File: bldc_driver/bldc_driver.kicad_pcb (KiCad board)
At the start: 2 copper layers, 74.9 x 56.1 mm, 77 parts, among them CON1 SAM-SWD-10, J1 I2C 1, Q1 PSMN0R925YLC, Q10 PSMN0R925YLC, Q11 PSMN0R925YLC, Q12 PSMN0R925YLC, Q2 PSMN0R925YLC, Q3 PSMN0R925YLC, Q4 PSMN0R925YLC, Q5 PSMN0R925YLC, Q6 PSMN0R925YLC, Q7 PSMN0R925YLC, Q8 PSMN0R925YLC, Q9 PSMN0R925YLC, U1 SAMD21E16L-MU, U2 INA199A2, U3 NCP5901, U4 NCP5901, U5 NCP5901, U6 INA199A2, U7 NCP5901, U8 NCP5901, U9 NCP5901

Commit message: well, missed commit when I fabricated the board, but I have extra parts here to try to fix it... honestly, I should just redesign with mosfet drivers intended for motor use that tolerate negative voltages
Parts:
- C10, C11, C12, C20, C21, C22: value 360nF -> 470nF
- R10, R11, R12, R17, R18, R19: value 4k -> 4.02k
- R2: value 3.9k -> 4.02k
- R5: value 1k -> 3k
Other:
- net class POWER_DRIVE added: clearance 0.2, trace_width 2, via_dia 0.6, via_drill 0.4

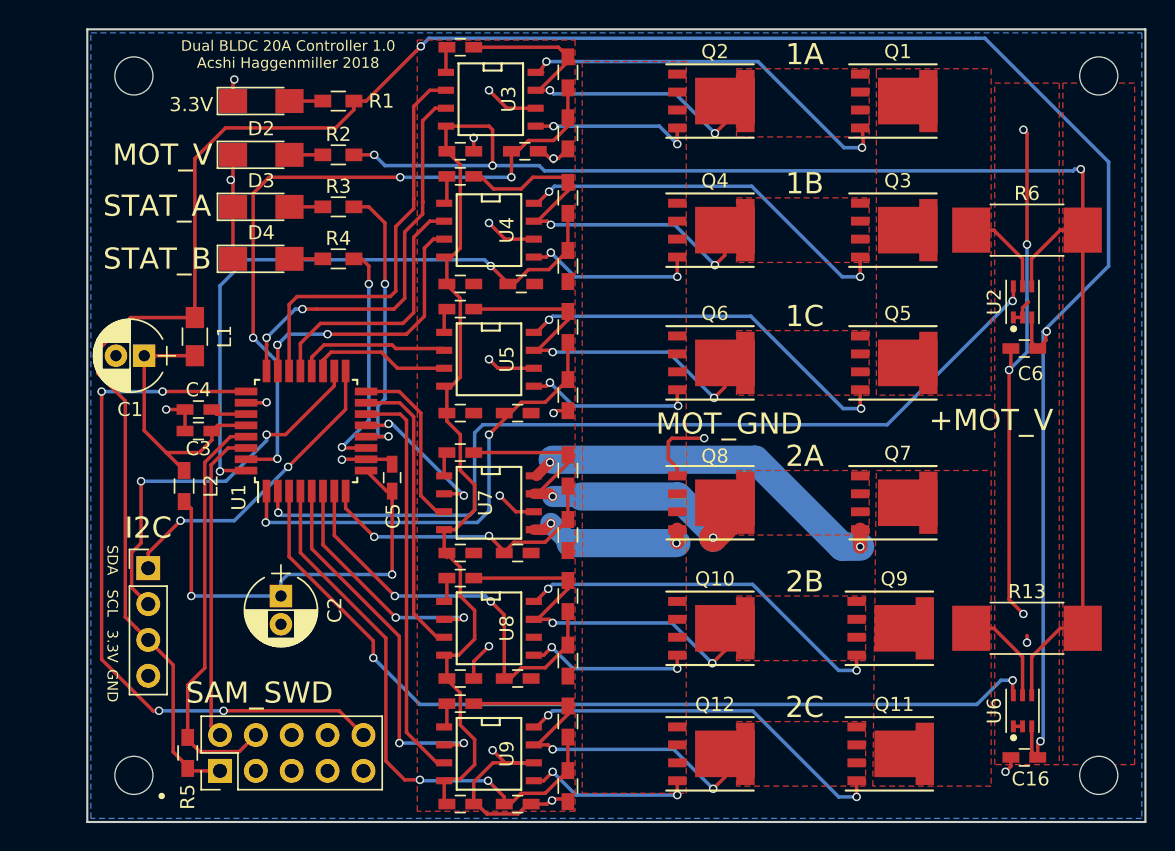
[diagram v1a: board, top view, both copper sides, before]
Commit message: finished v1.1 bldc, sent to make pcb; added components to quad rotor main board
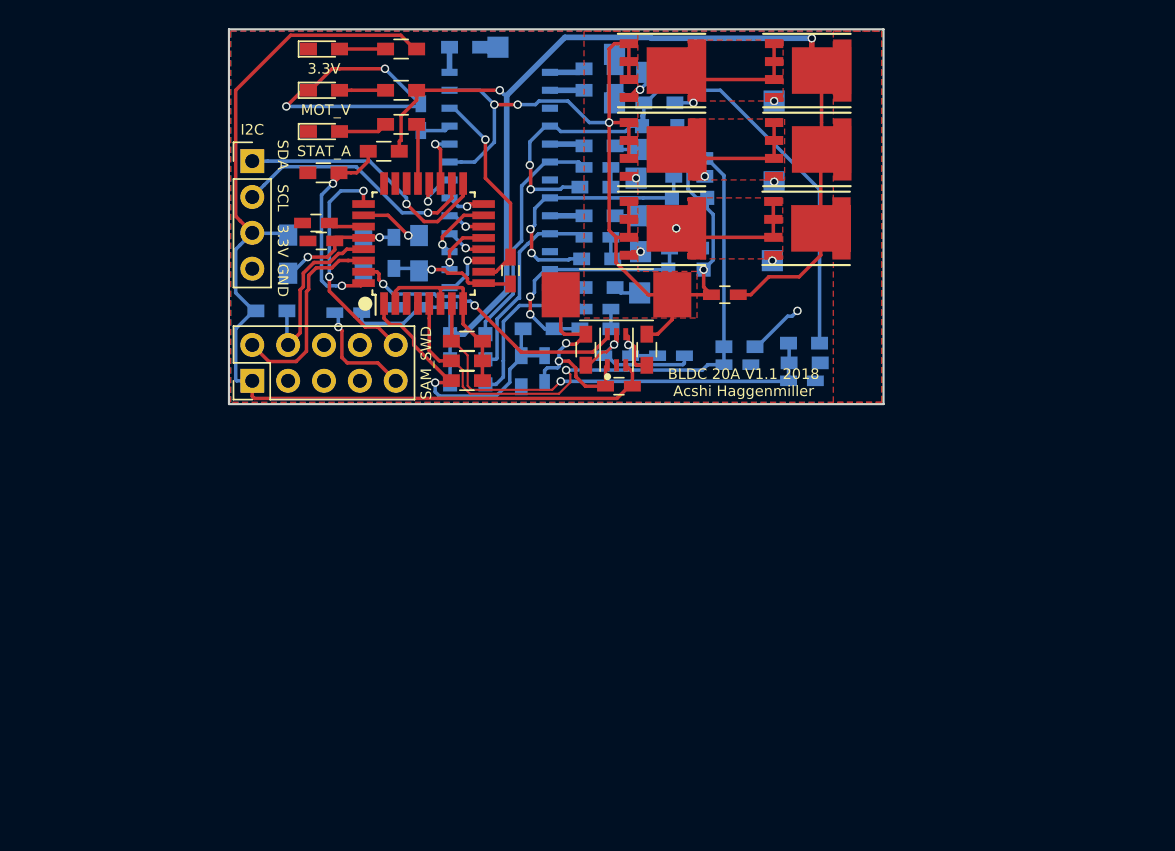
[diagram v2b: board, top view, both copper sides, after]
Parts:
- removed C20, C21, C22: 470nF, Capacitors_SMD:C_0603_HandSoldering
- removed C23, C24, C25: 1nF, Capacitors_SMD:C_0603_HandSoldering
- removed C6: 100nF, Capacitors_SMD:C_0603_HandSoldering
- removed Q10, Q11, Q12, Q7, Q8, Q9: PSMN0R925YLC, LFPAK:LFPAK_POWER_SO-8
- removed the REF** at (114.6, 125.2)
- removed the REF** at (114.6, 75.7)
- removed the REF** at (182.9, 75.7)
- removed the REF** at (182.9, 125.2)
- removed U4, U5, U7, U8, U9: NCP5901, SMD_Packages:SOIC-8-N
- removed U6: INA199A2, ina199a2:INA199A2
- added D5: DSS16UTR‎, Diodes_SMD:D_SOD-323_HandSoldering, B.Cu at (153.9, 84.3)
- added D6: DSS16UTR‎, Diodes_SMD:D_SOD-323_HandSoldering, B.Cu at (151.8, 79.2)
- added D7: DSS16UTR‎, Diodes_SMD:D_SOD-323_HandSoldering, B.Cu at (138.2, 94.0)
- added D8: DSS16UTR‎, Diodes_SMD:D_SOD-323_HandSoldering, B.Cu at (138.2, 95.8)
- added D9: DSS16UTR‎, Diodes_SMD:D_SOD-323_HandSoldering, B.Cu at (138.2, 97.5)
- added R20: 1R, Resistors_SMD:R_0603_HandSoldering, B.Cu at (147.2, 93.6)
- added R21: 1R, Resistors_SMD:R_0603_HandSoldering, B.Cu at (147.4, 88.6)
- added R22: 1R, Resistors_SMD:R_0603_HandSoldering, B.Cu at (147.2, 83.6)
- added R23: 20k, Resistors_SMD:R_0603_HandSoldering, B.Cu at (143.2, 93.6)
- added R24: 20k, Resistors_SMD:R_0603_HandSoldering, B.Cu at (153.9, 81.5)
- added R25: 20k, Resistors_SMD:R_0603_HandSoldering, B.Cu at (162.0, 94.6)
- added R26: 4.02k, Resistors_SMD:R_0603_HandSoldering, B.Cu at (142.0, 96.6)
- added R27: 4.02k, Resistors_SMD:R_0603_HandSoldering, B.Cu at (157.4, 94.9)
- added R28: 4.02k, Resistors_SMD:R_0603_HandSoldering, B.Cu at (162.1, 96.0)
- added R29: 20k, Resistors_SMD:R_0603_HandSoldering, F.Cu at (132.2, 81.0)
- added R30: 4.02k, Resistors_SMD:R_0603_HandSoldering, F.Cu at (128.0, 82.5)
- added REF**: Measurement_Point_Square-SMD-Pad_Small, Measurement_Points:Measurement_Point_Square-SMD-Pad_Small, B.Cu at (159.9, 83.2)
- added REF**: Measurement_Point_Square-SMD-Pad_Small, Measurement_Points:Measurement_Point_Square-SMD-Pad_Small, B.Cu at (148.6, 77.6)
- added REF**: Measurement_Point_Square-SMD-Pad_Small, Measurement_Points:Measurement_Point_Square-SMD-Pad_Small, B.Cu at (150.1, 82.9)
- added REF**: Measurement_Point_Square-SMD-Pad_Small, Measurement_Points:Measurement_Point_Square-SMD-Pad_Small, B.Cu at (140.3, 73.7)
- added REF**: Measurement_Point_Square-SMD-Pad_Small, Measurement_Points:Measurement_Point_Square-SMD-Pad_Small, B.Cu at (159.9, 77.5)
- added REF**: Measurement_Point_Square-SMD-Pad_Small, Measurement_Points:Measurement_Point_Square-SMD-Pad_Small, B.Cu at (159.8, 88.8)
- added REF**: Measurement_Point_Square-SMD-Pad_Small, Measurement_Points:Measurement_Point_Square-SMD-Pad_Small, B.Cu at (150.4, 88.1)
- added REF**: Measurement_Point_Square-SMD-Pad_Small, Measurement_Points:Measurement_Point_Square-SMD-Pad_Small, B.Cu at (150.4, 91.1)
- added REF**: Measurement_Point_Square-SMD-Pad_Small, Measurement_Points:Measurement_Point_Square-SMD-Pad_Small, B.Cu at (150.4, 85.6)
- added REF**: Measurement_Point_Square-SMD-Pad_Small, Measurement_Points:Measurement_Point_Square-SMD-Pad_Small, B.Cu at (150.4, 80.9)
- added REF**: Measurement_Point_Square-SMD-Pad_Small, Measurement_Points:Measurement_Point_Square-SMD-Pad_Small, B.Cu at (150.9, 75.4)
- added REF**: Measurement_Point_Square-SMD-Pad_Small, Measurement_Points:Measurement_Point_Square-SMD-Pad_Small, B.Cu at (148.6, 74.2)
- C1, C2: footprint Capacitors_THT:CP_Radial_D5.0mm_P2.00mm -> Capacitors_SMD:C_0805_HandSoldering; moved to B.Cu
- C10: value 470nF -> 1uF; moved to B.Cu
- C11: value 470nF -> 100nF
- C12: value 470nF -> 1nF; moved to B.Cu
- C13: value 1nF -> 1uF; moved to B.Cu
- C14, C15: value 1nF -> 0.68uF; moved to B.Cu
- C16: value 100nF -> 0.68uF; moved to B.Cu
- C17, C18, C19: value 100n -> 1nF; moved to B.Cu
- C7: value 100n -> 100nF
- C8, C9: value 100n -> 1uF; moved to B.Cu
- D1, D2, D3: footprint LEDs:LED_1206_HandSoldering -> LEDs:LED_0603_HandSoldering
- D4: value Red -> DSS16UTR‎; footprint LEDs:LED_1206_HandSoldering -> Diodes_SMD:D_SOD-323_HandSoldering; moved to B.Cu
- L1, L2, R4: moved to B.Cu
- R10, R12: value 4.02k -> 10
- R11: value 4.02k -> 2mR; footprint Resistors_SMD:R_0603_HandSoldering -> Resistors_SMD:R_2512_HandSoldering
- R13: value 2mR -> 10; footprint Resistors_SMD:R_2512_HandSoldering -> Resistors_SMD:R_0603_HandSoldering; moved to B.Cu
- R14, R15, R16: value 20k -> 4.7R; moved to B.Cu
- R17, R18, R19: value 4.02k -> 4.7R; moved to B.Cu
- R6: value 2mR -> 3k; footprint Resistors_SMD:R_2512_HandSoldering -> Resistors_SMD:R_0603_HandSoldering
- R7, R9: value 20k -> 10; moved to B.Cu
- R8: value 20k -> 3k
- U2: value INA199A2 -> INA199C2
- U3: value NCP5901 -> MIC4609; footprint SMD_Packages:SOIC-8-N -> SMD_Packages:SOIC-28; moved to B.Cu
- moved R19 52.8 mm to (138.0, 73.7), turned to 180 degrees
- moved C16 51.6 mm to (147.4, 82.2)
- moved R13 45.4 mm to (151.8, 77.6), turned to 180 degrees
- moved R18 42.0 mm to (147.5, 75.2), turned to 180 degrees
- moved R16 40.8 mm to (147.5, 80.6), turned to 180 degrees
- moved R6 40.7 mm to (138.1, 95.9), turned to 180 degrees
- moved C19 38.5 mm to (161.9, 97.3)
- moved R5 33.0 mm to (138.1, 97.3), turned to 180 degrees
- moved R17 31.6 mm to (147.5, 76.7), turned to 180 degrees
- moved D4 30.1 mm to (153.7, 89.4)
- moved J1 29.8 mm to (122.9, 81.7)
- moved C18 29.6 mm to (157.3, 96.1)
- moved U2 28.9 mm to (148.7, 95.1)
- moved CON1 27.7 mm to (122.9, 97.3)
- moved R15 27.0 mm to (147.5, 85.6), turned to 180 degrees
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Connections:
- C10 pad 1: Net-(C10-Pad1) -> GND
- C10 pad 2: /bldc_unit1/MOT_A -> /+V_MOTOR
- C11 pad 1: Net-(C11-Pad1) -> GND
- C11 pad 2: /bldc_unit1/MOT_B -> /+3.3V
- C12 pad 1: Net-(C12-Pad1) -> GND
- C12 pad 2: /bldc_unit1/MOT_C -> Net-(C12-Pad2)
- C13 pad 1: /bldc_unit1/MOTOR_A -> GND
- C13 pad 2: GND -> /+V_MOTOR
- C14 pad 1: /bldc_unit1/MOTOR_B -> Net-(C14-Pad1)
- C14 pad 2: GND -> Net-(C14-Pad2)
- C15 pad 1: /MOTOR1_C -> Net-(C15-Pad1)
- C15 pad 2: GND -> Net-(C15-Pad2)
- C16 pad 1: GND -> Net-(C16-Pad1)
- C16 pad 2: /+3.3V -> Net-(C16-Pad2)
- C17 pad 1: /+V_MOTOR -> /bldc_unit1/MOTOR_A
- C18 pad 1: /+V_MOTOR -> /bldc_unit1/MOTOR_B
- C19 pad 1: /+V_MOTOR -> /bldc_unit1/MOTOR_C
- C7 pad 2: GND -> /bldc_unit1/MOTOR_SHUNT
- C8 pad 1: /+V_MOTOR -> Net-(C8-Pad1)
- C8 pad 2: GND -> Net-(C8-Pad2)
- C9 pad 1: /+V_MOTOR -> Net-(C8-Pad1)
- C9 pad 2: GND -> Net-(C8-Pad2)
- CON1 pad 6: Net-(CON1-Pad6) -> (no net)
- CON1 pad 7: Net-(CON1-Pad7) -> (no net)
- CON1 pad 8: Net-(CON1-Pad8) -> (no net)
- D4 pad 1: GND -> /bldc_unit1/MOTF_A
- D4 pad 2: Net-(D4-Pad2) -> /bldc_unit1/MOTOR_SHUNT
- Q1 pad 1: /bldc_unit1/MOTOR_SHUNT -> /+V_MOTOR
- Q2 pad 3: GND -> /bldc_unit1/MOTOR_SHUNT
- Q3 pad 1: /bldc_unit1/MOTOR_SHUNT -> /+V_MOTOR
- Q4 pad 3: GND -> /bldc_unit1/MOTOR_SHUNT
- Q5 pad 1: /bldc_unit1/MOTOR_SHUNT -> /+V_MOTOR
- Q6 pad 3: GND -> /bldc_unit1/MOTOR_SHUNT
- R10 pad 1: GND -> Net-(C8-Pad2)
- R10 pad 2: /bldc_unit1/MOTOR_A -> /bldc_unit1/MOTOR_SHUNT
- R11 pad 1: /bldc_unit1/MOTOR_B -> GND
- R11 pad 2: GND -> /bldc_unit1/MOTOR_SHUNT
- R12 pad 1: /MOTOR1_C -> Net-(C8-Pad1)
- R13 pad 1: /bldc_unit2/MOTOR_SHUNT -> /bldc_unit1/MOT_C
- R13 pad 2: /+V_MOTOR -> /bldc_unit1/MOTF_C
- R14 pad 1: /bldc_unit2/MOTOR_A -> /bldc_unit1/GHA
- R14 pad 2: /bldc_unit2/MOT_A -> Net-(R14-Pad2)
- R15 pad 1: /bldc_unit2/MOTOR_B -> /bldc_unit1/GHB
- R15 pad 2: /bldc_unit2/MOT_B -> Net-(R15-Pad2)
- R16 pad 1: /MOTOR2_C -> /bldc_unit1/GHC
- R16 pad 2: /bldc_unit2/MOT_C -> Net-(R16-Pad2)
- R17 pad 1: GND -> /bldc_unit1/GLA
- R17 pad 2: /bldc_unit2/MOTOR_A -> Net-(R17-Pad2)
- R18 pad 1: /bldc_unit2/MOTOR_B -> /bldc_unit1/GLB
- R18 pad 2: GND -> Net-(R18-Pad2)
- R19 pad 1: /MOTOR2_C -> /bldc_unit1/GLC
- R19 pad 2: GND -> Net-(R19-Pad2)
- R3 pad 2: /STATUS_A -> /STATUS
- R4 pad 1: Net-(D4-Pad2) -> /+3.3V
- R4 pad 2: /STATUS_B -> /SWCLK
- R5 pad 1: /+3.3V -> /bldc_unit1/MOTOR_ZERO
- R5 pad 2: /SWCLK -> /bldc_unit1/MOTOR_A
- R6 pad 1: /bldc_unit1/MOTOR_SHUNT -> /bldc_unit1/MOTOR_ZERO
- R6 pad 2: /+V_MOTOR -> /bldc_unit1/MOTOR_B
- R7 pad 1: /bldc_unit1/MOTOR_A -> /bldc_unit1/MOTF_A
- R8 pad 1: /bldc_unit1/MOTOR_B -> /bldc_unit1/MOTOR_ZERO
- R8 pad 2: /bldc_unit1/MOT_B -> /bldc_unit1/MOTOR_C
- R9 pad 1: /MOTOR1_C -> /bldc_unit1/MOT_B
- R9 pad 2: /bldc_unit1/MOT_C -> /bldc_unit1/MOTF_B
- U1 pad 1: /MOTOR1_C -> /bldc_unit1/MOTOR_A
- U1 pad 11: /STATUS_B -> /bldc_unit1/IN_HA
- U1 pad 12: /STATUS_A -> /bldc_unit1/IN_LA
- U1 pad 13: /bldc_unit2/IN_A -> /bldc_unit1/IN_HB
- U1 pad 14: /bldc_unit2/ENABLE_C -> /bldc_unit1/IN_LB
- U1 pad 15: /bldc_unit2/ENABLE_B -> /bldc_unit1/IN_HC
- U1 pad 16: /bldc_unit2/ENABLE_A -> /bldc_unit1/IN_LC
- U1 pad 19: /bldc_unit1/ENABLE_C -> /bldc_unit1/ENABLE
- U1 pad 2: /CURRENT1 -> /bldc_unit1/MOTOR_ZERO
- U1 pad 20: /bldc_unit1/IN_C -> /bldc_unit1/~FAULT
- U1 pad 21: /bldc_unit1/IN_B -> /STATUS
- U1 pad 22: /bldc_unit1/IN_A -> (no net)
- U1 pad 23: /bldc_unit1/ENABLE_B -> (no net)
- U1 pad 24: /bldc_unit1/ENABLE_A -> (no net)
- U1 pad 3: /CURRENT2 -> (no net)
- U1 pad 31: /bldc_unit1/MOTOR_A -> /bldc_unit1/CURRENT
- U1 pad 32: /bldc_unit1/MOTOR_B -> Net-(R29-Pad2)
- U1 pad 4: /MOTOR2_C -> (no net)
- U1 pad 5: /bldc_unit2/IN_C -> /bldc_unit1/MOTOR_B
- U1 pad 6: /bldc_unit2/IN_B -> /bldc_unit1/MOTOR_ZERO
- U1 pad 7: /bldc_unit2/MOTOR_B -> /bldc_unit1/MOTOR_C
- U1 pad 8: /bldc_unit2/MOTOR_A -> /bldc_unit1/MOTOR_ZERO
- U2 pad 4: /+V_MOTOR -> Net-(C8-Pad2)
- U2 pad 5: /bldc_unit1/MOTOR_SHUNT -> Net-(C8-Pad1)
- U2 pad 6: /CURRENT1 -> /bldc_unit1/CURRENT
- U3 pad 1: Net-(C10-Pad1) -> /+V_MOTOR
- U3 pad 2: /bldc_unit1/IN_A -> /bldc_unit1/IN_HA
- U3 pad 3: /bldc_unit1/ENABLE_A -> /bldc_unit1/IN_HB
- U3 pad 4: /+V_MOTOR -> /bldc_unit1/IN_HC
- U3 pad 5: /bldc_unit1/GLA -> /bldc_unit1/IN_LA
- U3 pad 6: GND -> /bldc_unit1/IN_LB
- U3 pad 7: /bldc_unit1/MOT_A -> /bldc_unit1/IN_LC
- U3 pad 8: /bldc_unit1/GHA -> /bldc_unit1/~FAULT
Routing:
- net /+3.3V: track 176.3 -> 71.4 mm, vias 3 -> 0
- net /+V_MOTOR: track 162.3 -> 91.1 mm, vias 3 -> 2
- net /bldc_unit1/MOTOR_SHUNT: track 6.42 -> 71.6 mm, vias 0 -> 4
- net /CURRENT1: track 64.0 -> 0.00 mm, vias 2 -> 0
- net /CURRENT2: track 62.9 -> 0.00 mm, vias 2 -> 0
- net /bldc_unit1/MOTF_C: track 0.00 -> 44.9 mm, vias 0 -> 2
- net /MOTOR2_C: track 39.6 -> 0.00 mm, vias 2 -> 0
- net /MOTOR1_C: track 34.3 -> 0.00 mm, vias 2 -> 0
- net /RESET: track 50.0 -> 16.3 mm, vias 4 -> 2
- net GND: track 101.5 -> 69.2 mm, vias 21 -> 8
- net /bldc_unit1/MOTOR_C: track 0.00 -> 32.2 mm, vias 0 -> 1
- net /bldc_unit2/MOTOR_B: track 29.9 -> 0.00 mm, vias 2 -> 0
- net /bldc_unit1/IN_A: track 29.0 -> 0.00 mm
- net /bldc_unit2/ENABLE_C: track 28.7 -> 0.00 mm
- net /bldc_unit1/ENABLE_A: track 28.5 -> 0.00 mm, vias 2 -> 0
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- removed copper zone on F.Cu, net /bldc_unit2/MOTOR_SHUNT
- removed copper zone on F.Cu, net /bldc_unit2/MOT_A
- removed copper zone on F.Cu, net /bldc_unit2/MOT_B
- removed copper zone on F.Cu, net /bldc_unit2/MOT_C
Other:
- board size 74.9 x 56.1 mm -> 46.4 x 26.5 mm
- net class Default: clearance 0.2 -> 0.13
- net class POWER_DRIVE removed
- rule pad_to_mask_clearance: 0.2 -> 0.06
- rule trace_clearance: 0.2 -> 0.13
- rule trace_min: 0.2 -> 0.15
- board text added: "1"
- board text added: "2"
- board text added: "3"
- board text added: "4"
- board text added: "5"
- board text added: "6"
- board text added: "BLDC 20A V1.1 2018 Acshi Haggenmiller"
- board text removed: "+MOT_V"
- board text removed: "1A"
- board text removed: "1B"
- board text removed: "1C"
- board text removed: "2A"
- board text removed: "2B"
- board text removed: "2C"
- board text removed: "Dual BLDC 20A Controller 1.0 Acshi Haggenmiller 2018"
- board text removed: "MOT_GND"
- board text removed: "STAT_B"

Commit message: thinking about adding extra clamping protection to sense pins
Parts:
- added D10: D_Schottky_x2_Serial_AKC, Package_TO_SOT_SMD:SOT-23_Handsoldering, F.Cu at (109.5, 93.3)
- added D11: D_Schottky_x2_Serial_AKC, Package_TO_SOT_SMD:SOT-23_Handsoldering, F.Cu at (109.5, 96.9)
- added D12: D_Schottky_x2_Serial_AKC, Package_TO_SOT_SMD:SOT-23_Handsoldering, F.Cu at (115.0, 93.3)
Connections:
- CON1 pad 6: (no net) -> Net-(CON1-Pad6)
- CON1 pad 7: (no net) -> Net-(CON1-Pad7)
- CON1 pad 8: (no net) -> Net-(CON1-Pad8)
- U1 pad 22: (no net) -> Net-(U1-Pad22)
- U1 pad 23: (no net) -> Net-(U1-Pad23)
- U1 pad 24: (no net) -> Net-(U1-Pad24)
- U1 pad 3: (no net) -> Net-(U1-Pad3)
- U1 pad 4: (no net) -> Net-(U1-Pad4)

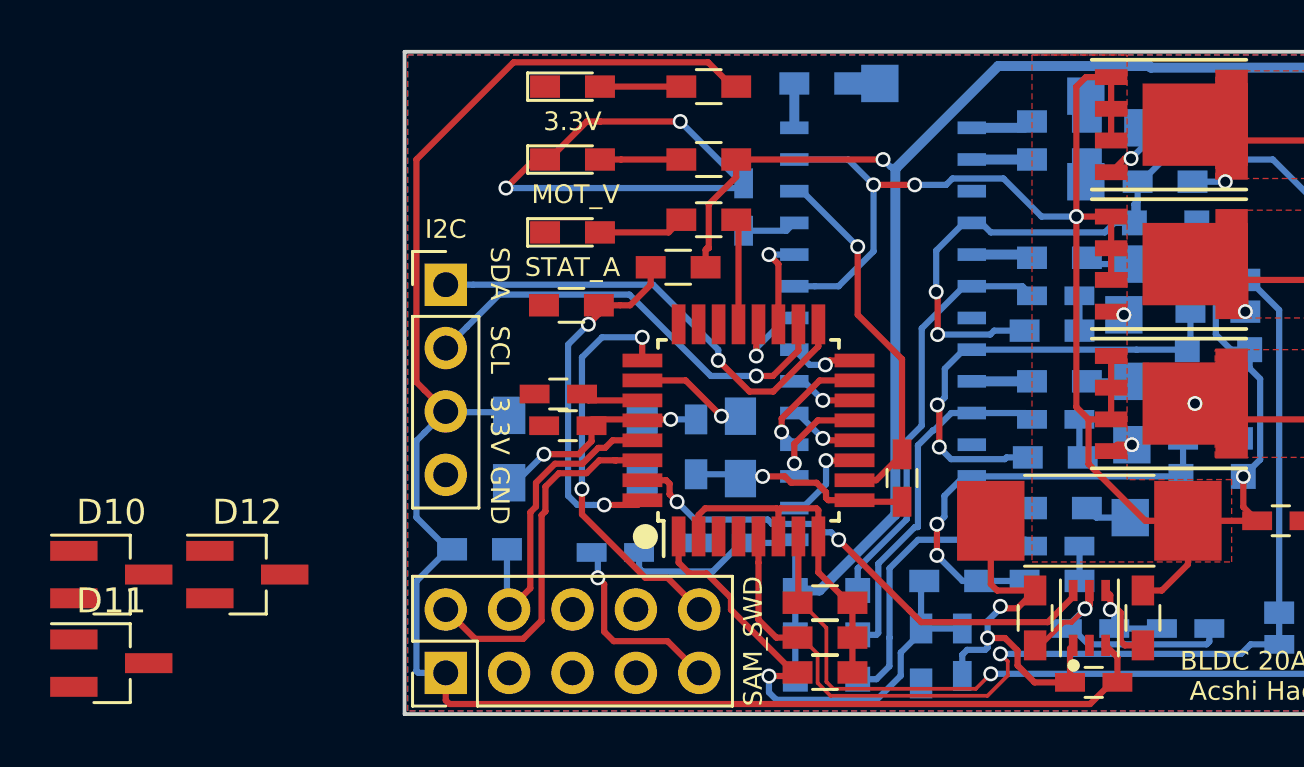
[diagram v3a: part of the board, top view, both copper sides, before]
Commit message: fixed mic4609 footprint, fixed isns bug by giving it divided voltage for current measurement, did not update all pcb footprints to match new ones in schematic from the new kicad library
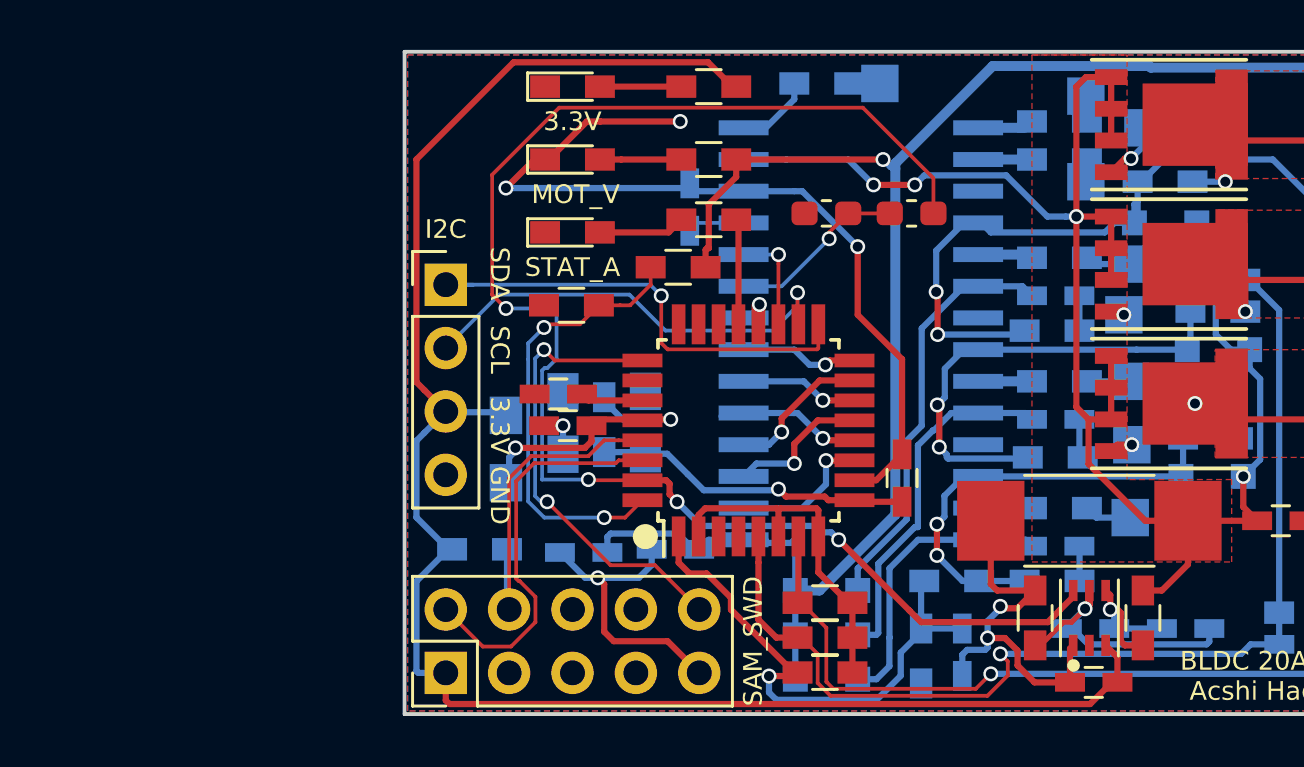
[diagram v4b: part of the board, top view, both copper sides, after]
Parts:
- removed D10, D11, D12: D_Schottky_x2_Serial_AKC, Package_TO_SOT_SMD:SOT-23_Handsoldering
- added R31: 15K, Resistor_SMD:R_0603_1608Metric_Pad1.05x0.95mm_HandSolder, F.Cu at (141.6, 78.9)
- added R32: 2.2K, Resistor_SMD:R_0603_1608Metric_Pad1.05x0.95mm_HandSolder, F.Cu at (138.2, 78.9)
- U3: footprint SMD_Packages:SOIC-28 -> Package_SO:SOIC-28W_7.5x17.9mm_P1.27mm
- moved C2 3.94 mm to (130.9, 87.2)
- moved L2 3.79 mm to (129.3, 87.3)
- moved C1 3.36 mm to (127.6, 87.3)
- moved C12 2.16 mm to (132.7, 78.6)
- moved C13 1.93 mm to (132.1, 92.3)
- moved C10 1.27 mm to (128.5, 92.5)
- moved U3 0.89 mm to (139.6, 83.7), turned to 0 degrees
- moved L1 0.13 mm to (125.3, 88.3)
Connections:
- U3 pad 9: /bldc_unit1/MOTOR_SHUNT -> Net-(R31-Pad1)
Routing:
- net /bldc_unit1/CURRENT: track 20.5 -> 60.7 mm, vias 2 -> 4
- net Net-(R31-Pad1): track 0.00 -> 7.22 mm, vias 0 -> 1
- net /bldc_unit1/MOTOR_SHUNT: track 71.6 -> 67.0 mm
- net Net-(C2-Pad1): track 8.92 -> 12.8 mm
- net Net-(C1-Pad1): track 9.99 -> 13.5 mm
- net Net-(R29-Pad2): track 14.5 -> 17.8 mm
- net /bldc_unit1/IN_HB: track 4.11 -> 7.01 mm
- net /RESET: track 16.3 -> 18.8 mm
- net /+V_MOTOR: track 91.1 -> 93.2 mm
- net /bldc_unit1/IN_LB: track 2.73 -> 4.76 mm
- net /bldc_unit1/IN_HA: track 3.76 -> 5.80 mm
- net /bldc_unit1/IN_LA: track 2.87 -> 4.77 mm
- net /bldc_unit1/~FAULT: track 3.65 -> 1.81 mm
- net /SWDIO: track 14.5 -> 16.0 mm
- net /bldc_unit1/IN_LC: track 2.74 -> 3.83 mm
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
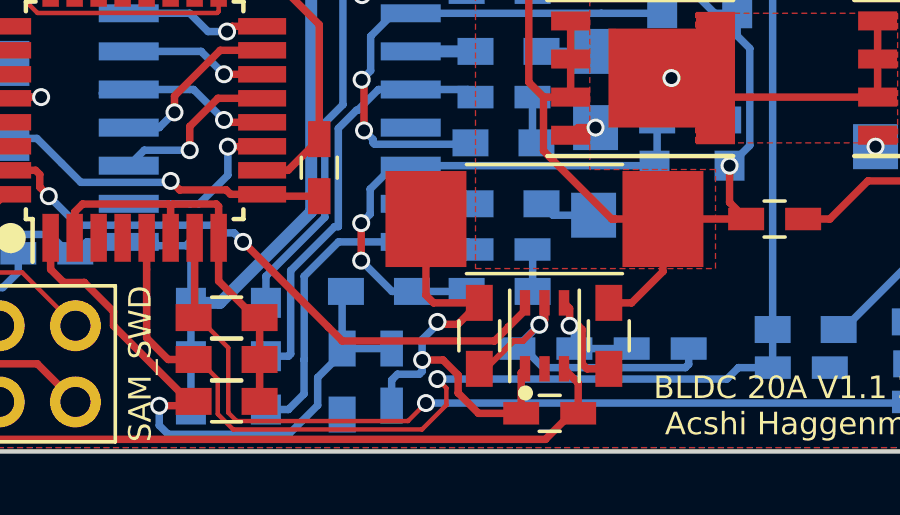
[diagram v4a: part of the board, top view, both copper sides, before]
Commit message: added logic level converter for 9 dof imu sensor. some setup for both sensors to use spi
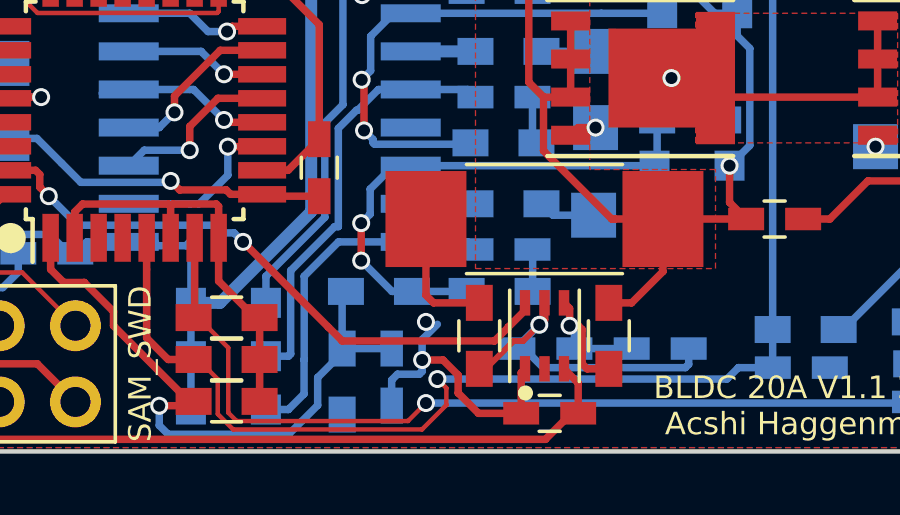
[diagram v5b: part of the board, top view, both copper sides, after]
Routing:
- net GND: track 69.9 -> 68.2 mm
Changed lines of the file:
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@@
     (thickness 1.6)
     (drawings 28)
-    (tracks 650)
+    (tracks 648)
     (zones 0)
     (modules 84)
@@
   (segment (start 158.537 94.869) (end 158.687 94.869) (width 0.25) (layer B.Cu) (net 2))
   (segment (start 158.687 94.869) (end 160.846 92.71) (width 0.25) (layer B.Cu) (net 2))
-  (segment (start 145.161 94.695) (end 145.843 94.695) (width 0.25) (layer F.Cu) (net 2))
-  (segment (start 145.843 94.695) (end 146.558 93.98) (width 0.25) (layer F.Cu) (net 2))
   (segment (start 144.653 95.885) (end 144.653 95.203) (width 0.25) (layer B.Cu) (net 2))
   (segment (start 144.653 95.203) (end 145.161 94.695) (width 0.25) (layer B.Cu) (net 2))
-  (via (at 145.161 94.615) (size 0.6) (drill 0.4) (layers F.Cu B.Cu) (net 2))
+  (via (at 144.78 94.615) (size 0.6) (drill 0.4) (layers F.Cu B.Cu) (net 2))
   (segment (start 144.653 95.885) (end 144.653 96.266) (width 0.25) (layer B.Cu) (net 2))
   (segment (start 144.653 96.266) (end 144.559999 96.359001) (width 0.25) (layer B.Cu) (net 2))
@@
       )
     )
+  )
+  (zone (net 0) (net_name "") (layer F.Cu) (hatch edge 0.508)
+    (connect_pads (clearance 0.2))
+    (min_thickness 0.2)
+    (keepout (tracks allowed) (vias allowed) (copperpour not_allowed))
+    (fill (arc_segments 16) (thermal_gap 0.2) (thermal_bridge_width 0.5))
+    (polygon
+      (pts
+        (xy 151.384 94.615) (xy 153.162 92.837) (xy 144.399 92.837) (xy 144.399 93.853) (xy 145.415 94.615)
+      )
+    )
